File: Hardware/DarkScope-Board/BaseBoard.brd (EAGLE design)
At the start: 118.4 x 80 mm, 87 parts, among them IC1 7805DT, IC2 REG1117, IC3 7905, J1 DCJ0202, Q1 8MHz, T2 9014, U1 STM32F103CBT6, X1 TSW-102-07-G-S, X2 TSW-102-07-G-S, X3 MINI-USB-32005-301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

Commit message: CP Component Placements
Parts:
- removed JP1, JP2: (no value), pinhead:1X02
- moved TP15 203.8 mm to (103.5, 30.5), turned to 90 degrees
- moved TP14 192.1 mm to (86.4, 6.35)
- moved L3 186.9 mm to (102.9, 13.3), turned to 90 degrees
- moved TP13 186.4 mm to (97.2, 29.2)
- moved TP12 177.6 mm to (94.0, 29.2), turned to 90 degrees
- moved R7 163.0 mm to (94.0, 5.71), turned to 180 degrees
- moved R14 156.9 mm to (63.5, 17.8), turned to 90 degrees
- moved R8 155.4 mm to (100.3, 5.71)
- moved R6 151.1 mm to (76.8, 7.62)
- moved R13 148.8 mm to (63.5, 23.5), turned to 270 degrees
- moved D2 143.2 mm to (90.8, 14.0), turned to 270 degrees
- moved C15 140.2 mm to (103.5, 24.8), turned to 90 degrees
- moved C14 120.2 mm to (95.2, 14.0), turned to 90 degrees
- moved R1 112.8 mm to (57.8, 34.9), turned to 180 degrees
- moved R2 112.1 mm to (55.2, 44.5)
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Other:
- board size 118.4 x 80 mm -> 110.2 x 80 mm

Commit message: Cp BB Placement Completed
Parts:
- moved TP7 194.2 mm to (100.3, 46.4)
- moved TP8 184.3 mm to (67.9, 9.53)
- moved TP5 179.0 mm to (93.3, 43.2)
- moved TP10 158.0 mm to (82.5, 37.5)
- moved TP3 156.5 mm to (74.3, 32.4), turned to 90 degrees
- moved TP11 148.6 mm to (94.0, 65.4)
- moved TP6 125.6 mm to (33.7, 50.8)
- moved TP4 125.2 mm to (27.9, 26.0)
- moved TP18 114.0 mm to (29.2, 6.99)
- moved TP20 110.7 mm to (29.8, 21.0)
- moved TP1 108.2 mm to (41.9, 55.2)
- moved TP19 103.5 mm to (24.8, 21.0)
- moved TP2 90.4 mm to (15.9, 54.6)
- moved R17 11.4 mm to (13.3, 17.8), turned to 270 degrees
- moved C8 8.84 mm to (21.0, 59.1)
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
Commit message: UnRouted Board Bkp
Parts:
- moved JP6 25.0 mm to (45.7, 60.3), turned to 0 degrees
- moved X2 10.3 mm to (73.0, 73.0), turned to 0 degrees
- moved D2 5.24 mm to (85.7, 12.7)
- moved C11 5.24 mm to (94.0, 59.1)
- moved C12 5.24 mm to (94.0, 38.7)
- moved C9 5.24 mm to (72.4, 41.3)
- moved IC1 5.24 mm to (80.0, 59.1)
- moved IC2 5.24 mm to (80.6, 41.9)
- moved JMP2 5.24 mm to (88.3, 36.2)
- moved L2 5.24 mm to (85.1, 50.2)
- moved L4 5.24 mm to (81.9, 25.4)
- moved SJ3 5.24 mm to (78.7, 50.2)
- moved TP10 5.24 mm to (77.5, 36.2)
- moved TP5 5.24 mm to (88.3, 41.9)
- moved C13 5.24 mm to (78.1, 10.2)
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- renumbered JP4 to SIGGEN, JP5 to UART
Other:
- board size 110.2 x 80 mm -> 101.9 x 80 mm
- board text added: "-5V PSU"
- board text added: "9V Max"
- board text added: "9V/5V PSU"
- board text added: "Buttons Port"
- board text added: "By Yatin Khurana, MAIT 00514807319"
- board text added: "DB2 Port"
- board text added: "Expansion/Aux Port"
- board text added: "Reset"
- board text added: "STM32 Based Oscilloscope"
- board text added: "SWD"

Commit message: CP BB PCB Draft
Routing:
- net GND: track 0.00 -> 634.1 mm, vias 0 -> 4
- net +3V3: track 0.00 -> 334.0 mm, vias 0 -> 8
- net +5V: track 0.00 -> 211.5 mm, vias 0 -> 1
- net V-MON: track 0.00 -> 176.8 mm, vias 0 -> 4
- net LCD_NRESET: track 0.00 -> 129.3 mm, vias 0 -> 2
- net USBDP: track 0.00 -> 127.8 mm, vias 0 -> 3
- net USBDM: track 0.00 -> 124.8 mm, vias 0 -> 4
- net +12V: track 0.00 -> 123.9 mm, vias 0 -> 1
- net LCD_NRD: track 0.00 -> 121.1 mm, vias 0 -> 3
- net -5V: track 0.00 -> 113.9 mm
- net NRST: track 0.00 -> 113.6 mm, vias 0 -> 3
- net TESTSIG: track 0.00 -> 109.7 mm, vias 0 -> 4
- net VGEN: track 0.00 -> 109.5 mm, vias 0 -> 3
- net DB2: track 0.00 -> 109.1 mm, vias 0 -> 4
- net SWCLK: track 0.00 -> 93.0 mm, vias 0 -> 2
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- added copper zone on layer 1, net GND
- added copper zone on layer 16, net GND

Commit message: Added Mounting Holes
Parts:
- added U$1, U$2, U$3, U$4: (no value), special-drill:DRILL_0.1560
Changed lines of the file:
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@@
 <attribute name="VALUE" x="10.795" y="64.135" size="1.27" layer="27"/>
 </element>
+<element name="U$1" library="special-drill" library_urn="urn:adsk.eagle:library:366" package="DRILL_0.1560" value="" x="4.445" y="4.445" smashed="yes"/>
+<element name="U$2" library="special-drill" library_urn="urn:adsk.eagle:library:366" package="DRILL_0.1560" value="" x="2.47865" y="67.02668125" smashed="yes"/>
+<element name="U$3" library="special-drill" library_urn="urn:adsk.eagle:library:366" package="DRILL_0.1560" value="" x="98.425" y="63.5" smashed="yes"/>
+<element name="U$4" library="special-drill" library_urn="urn:adsk.eagle:library:366" package="DRILL_0.1560" value="" x="67.31" y="15.24" smashed="yes"/>
 </elements>
 <signals>

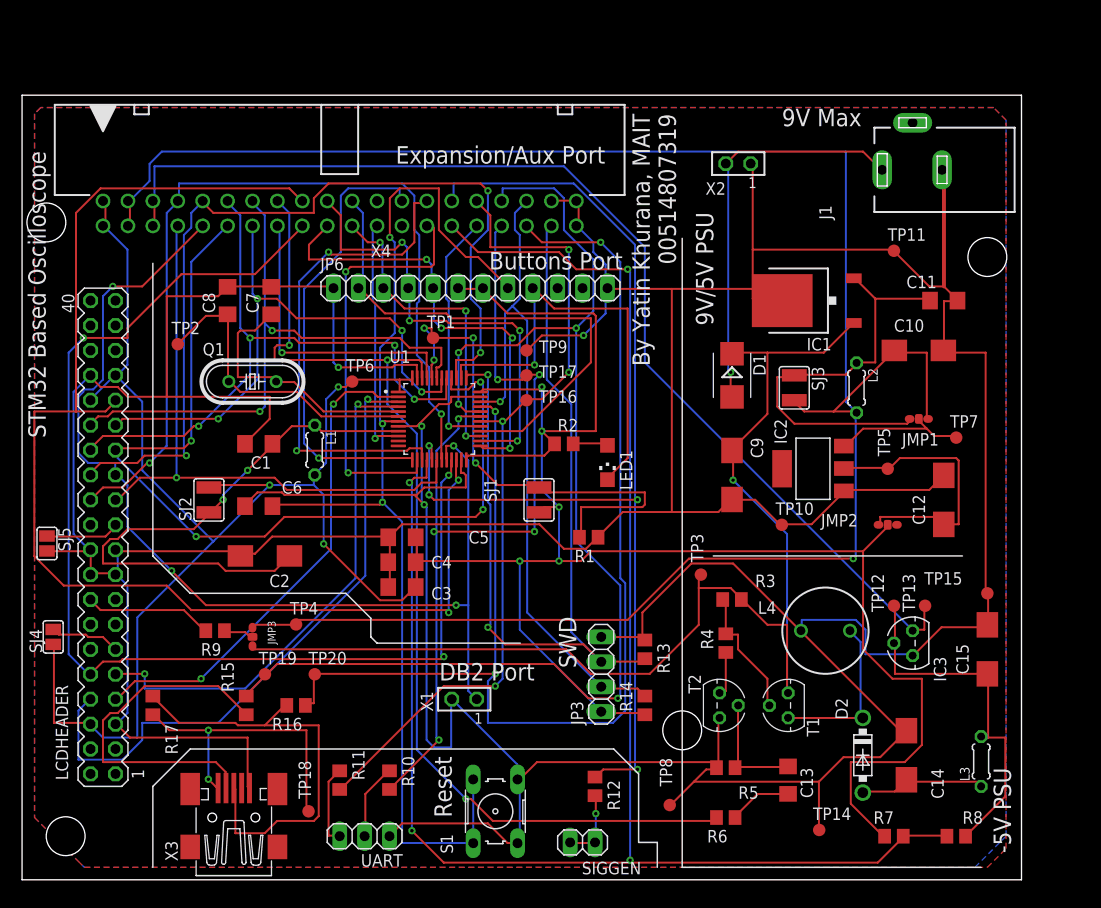
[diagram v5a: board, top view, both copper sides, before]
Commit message: Added PCB Holes for Mounting
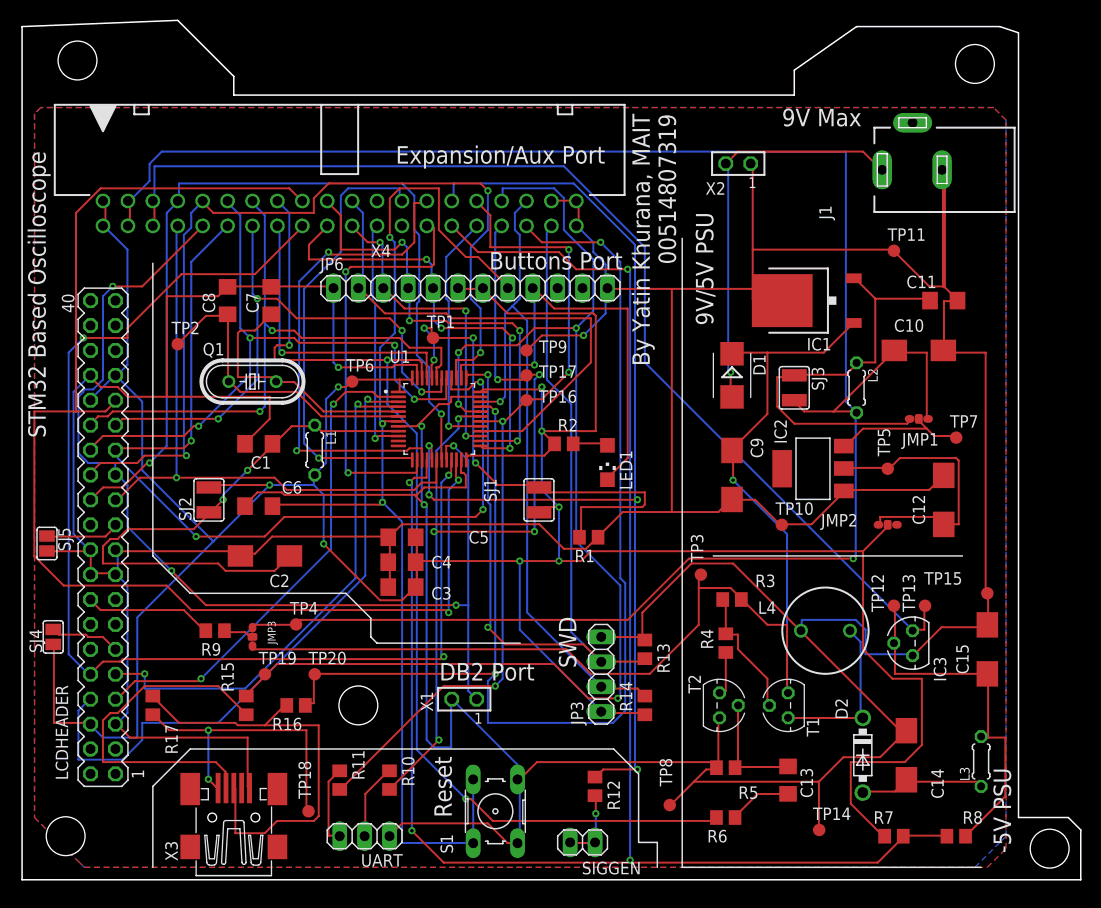
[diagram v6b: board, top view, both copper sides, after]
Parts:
- added U$5: (no value), special-drill:DRILL_0.1560
- moved U$4 33.1 mm to (34.3, 17.8)
- moved U$3 19.7 mm to (97.2, 83.2)
- moved U$2 16.8 mm to (5.65, 83.5)
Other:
- board size 101.9 x 80 mm -> 108 x 87.6 mm
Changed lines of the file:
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@@
 <board>
 <plain>
-<wire x1="0" y1="0" x2="101.905" y2="0" width="0" layer="20"/>
-<wire x1="101.905" y1="0" x2="101.905" y2="80" width="0" layer="20"/>
-<wire x1="101.905" y1="80" x2="0" y2="80" width="0" layer="20"/>
-<wire x1="0" y1="80" x2="0" y2="0" width="0" layer="20"/>
 <wire x1="67.31" y1="65.405" x2="67.31" y2="1.27" width="0.1524" layer="25"/>
 <wire x1="67.31" y1="1.27" x2="97.79" y2="1.27" width="0.1524" layer="25"/>
@@
 <wire x1="64.77" y1="3.81" x2="64.77" y2="1.27" width="0.1524" layer="25"/>
 <text x="77.47" y="76.835" size="1.778" layer="25">9V Max</text>
+<wire x1="0" y1="0" x2="0" y2="86.995" width="0.1524" layer="20"/>
+<wire x1="0" y1="86.995" x2="15.875" y2="87.63" width="0.1524" layer="20"/>
+<wire x1="15.875" y1="87.63" x2="21.59" y2="81.915" width="0.1524" layer="20"/>
+<wire x1="21.59" y1="81.915" x2="21.59" y2="80.01" width="0.1524" layer="20"/>
+<wire x1="21.59" y1="80.01" x2="78.74" y2="80.01" width="0.1524" layer="20"/>
+<wire x1="78.74" y1="80.01" x2="78.74" y2="82.55" width="0.1524" layer="20"/>
+<wire x1="78.74" y1="82.55" x2="85.09" y2="86.995" width="0.1524" layer="20"/>
+<wire x1="85.09" y1="86.995" x2="99.695" y2="86.995" width="0.1524" layer="20"/>
+<wire x1="99.695" y1="86.995" x2="101.6" y2="86.36" width="0.1524" layer="20"/>
+<wire x1="101.6" y1="86.36" x2="101.6" y2="6.35" width="0.1524" layer="20"/>
+<wire x1="107.95" y1="0" x2="0" y2="0" width="0.1524" layer="20"/>
+<wire x1="101.6" y1="6.35" x2="106.68" y2="6.35" width="0.1524" layer="20"/>
+<wire x1="106.68" y1="6.35" x2="107.95" y2="5.08" width="0.1524" layer="20"/>
+<wire x1="107.95" y1="5.08" x2="107.95" y2="0" width="0.1524" layer="20"/>
 </plain>
 <attributes>
@@
 </element>
 <element name="U$1" library="special-drill" library_urn="urn:adsk.eagle:library:366" package="DRILL_0.1560" value="" x="4.445" y="4.445" smashed="yes"/>
-<element name="U$2" library="special-drill" library_urn="urn:adsk.eagle:library:366" package="DRILL_0.1560" value="" x="2.47865" y="67.02668125" smashed="yes"/>
-<element name="U$3" library="special-drill" library_urn="urn:adsk.eagle:library:366" package="DRILL_0.1560" value="" x="98.425" y="63.5" smashed="yes"/>
-<element name="U$4" library="special-drill" library_urn="urn:adsk.eagle:library:366" package="DRILL_0.1560" value="" x="67.31" y="15.24" smashed="yes"/>
+<element name="U$2" library="special-drill" library_urn="urn:adsk.eagle:library:366" package="DRILL_0.1560" value="" x="5.65365" y="83.53668125" smashed="yes"/>
+<element name="U$3" library="special-drill" library_urn="urn:adsk.eagle:library:366" package="DRILL_0.1560" value="" x="97.155" y="83.185" smashed="yes"/>
+<element name="U$4" library="special-drill" library_urn="urn:adsk.eagle:library:366" package="DRILL_0.1560" value="" x="34.29" y="17.78" smashed="yes"/>
+<element name="U$5" library="special-drill" library_urn="urn:adsk.eagle:library:366" package="DRILL_0.1560" value="" x="104.775" y="3.175" smashed="yes"/>
 </elements>
 <signals>

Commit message: Drafted Sch for Probe Board
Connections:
- removed net VSENSEL3: X4.24
- removed net VSENSEL4: X4.25
- net VSENSEL1: now also X4.24
- net VSENSEL2: now also X4.25
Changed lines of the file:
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@@
 <drawing>
 <settings>
-<setting alwaysvectorfont="yes"/>
+<setting alwaysvectorfont="no"/>
 <setting verticaltext="up"/>
 </settings>
@@
 <signal name="VSENSEL2">
 <contactref element="U1" pad="11"/>
+<contactref element="X4" pad="25"/>
+<wire x1="38.365" y1="44.74" x2="38.735" y2="66.675" width="0" layer="19" extent="1-1"/>
 </signal>
 <signal name="VSENSEL1">
 <contactref element="U1" pad="12"/>
+<contactref element="X4" pad="24"/>
+<wire x1="38.365" y1="44.24" x2="36.195" y2="69.215" width="0" layer="19" extent="1-1"/>
 </signal>
 <signal name="CPLSEL">
@@
 <contactref element="JP6" pad="11"/>
 </signal>
-<signal name="VSENSEL3">
-<contactref element="X4" pad="24"/>
-</signal>
-<signal name="VSENSEL4">
-<contactref element="X4" pad="25"/>
-</signal>
 </signals>

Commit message: Fixed baseboard
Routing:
- net GND: track 634.1 -> 5.47 mm, vias 4 -> 0
- net VSENSEL1: track 0.00 -> 110.3 mm, vias 0 -> 3
- net +5V: track 211.5 -> 144.4 mm, vias 1 -> 5
- net ADCIN2: track 42.8 -> 108.4 mm, vias 2 -> 3
- net V-MON: track 176.8 -> 116.8 mm, vias 4 -> 2
- net +3V3: track 334.0 -> 275.8 mm, vias 8 -> 10
- net USBDP: track 127.8 -> 76.2 mm, vias 3 -> 2
- net DB5: track 65.0 -> 114.8 mm, vias 4 -> 2
- net VSENSEL2: track 0.00 -> 45.6 mm, vias 0 -> 1
- net N$21: track 54.0 -> 94.1 mm, vias 4 -> 7
- net DB0: track 62.5 -> 98.7 mm, vias 1 -> 3
- net LCD_NRD: track 121.1 -> 91.5 mm, vias 3 -> 4
- net SWCLK: track 93.0 -> 64.3 mm
- net N$29: track 36.1 -> 8.81 mm
- net LCD_NRESET: track 129.3 -> 103.7 mm, vias 2 -> 3
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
